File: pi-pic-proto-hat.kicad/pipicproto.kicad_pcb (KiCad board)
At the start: 2 copper layers, 65 x 56 mm, 20 parts, among them J1 RUN/~PGM~, J10 Conn_01x13_Male, J22 Conn_01x13_Male, J6 Barrel_Jack_Switch, J7 Conn_01x24_Male, J8 Conn_01x06_Male, J9 Conn_01x02_Male, P1 Conn_02x20_Odd_Even, Q1 IRF4905, U1 PIC12F675-IP

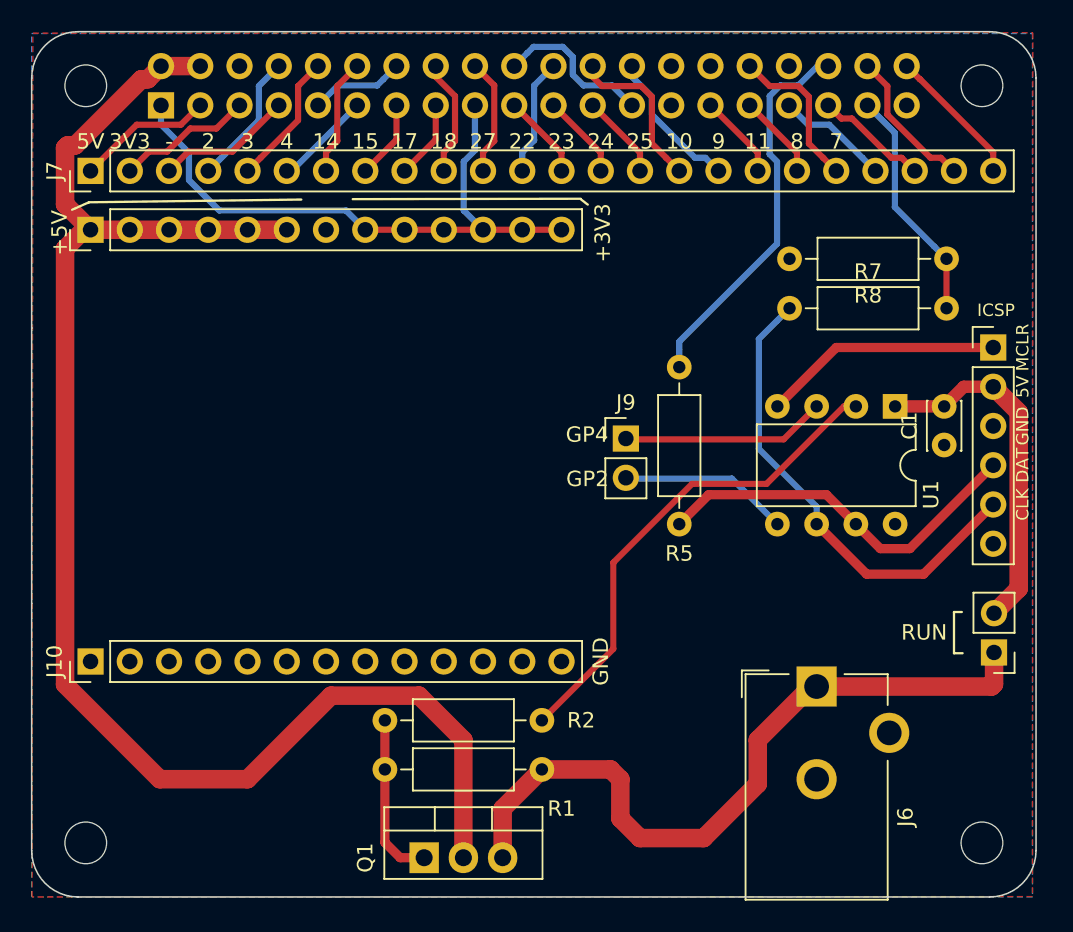
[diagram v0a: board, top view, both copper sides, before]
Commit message: V2.08: migrate to SMD for PIC
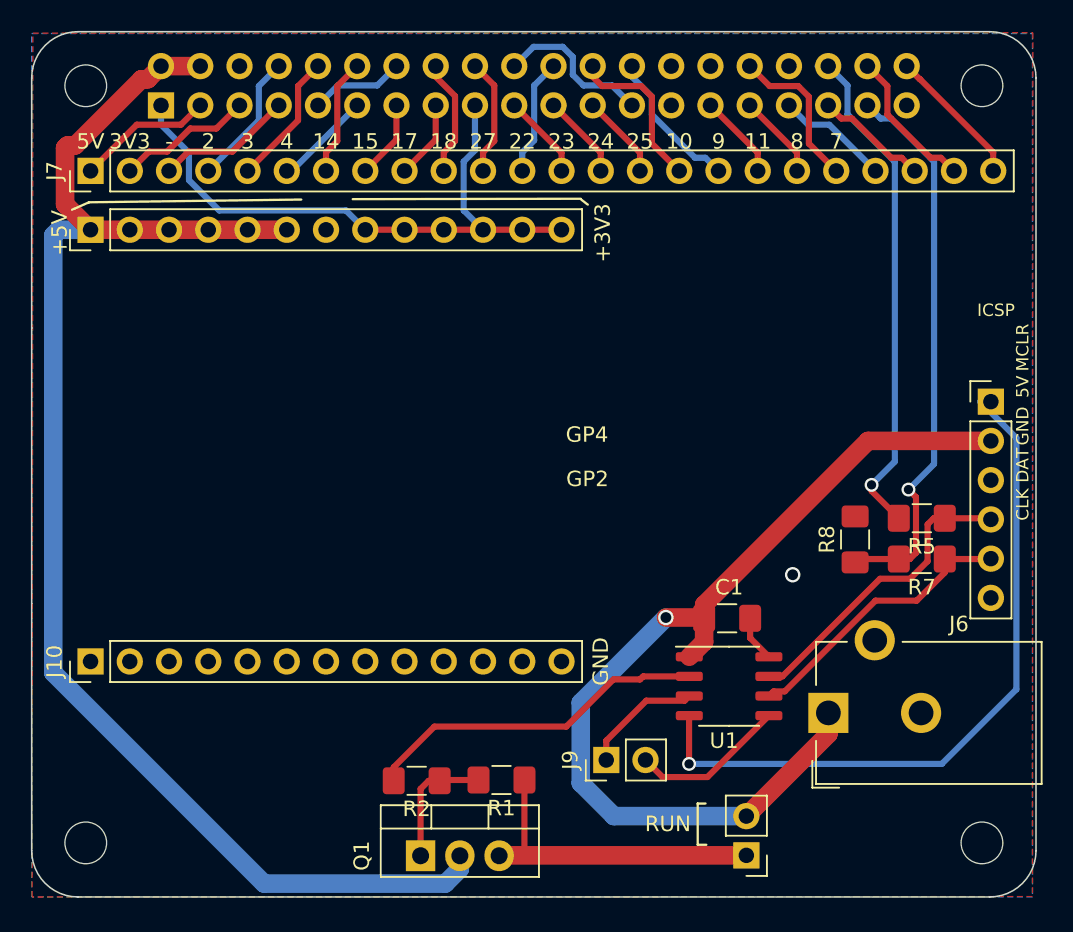
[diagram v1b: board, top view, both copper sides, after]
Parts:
- C1: footprint Capacitor_THT:C_Disc_D3.0mm_W2.0mm_P2.50mm -> Capacitor_SMD:C_1206_3216Metric_Pad1.42x1.75mm_HandSolder
- R1, R2, R5, R7, R8: footprint Resistor_THT:R_Axial_DIN0207_L6.3mm_D2.5mm_P10.16mm_Horizontal -> Resistor_SMD:R_1206_3216Metric_Pad1.42x1.75mm_HandSolder
- U1: footprint Package_DIP:DIP-8_W7.62mm -> Package_SO:SO-8_3.9x4.9mm_P1.27mm
- moved U1 21.1 mm to (245.1, 136.4), turned to 0 degrees
- moved J9 20.8 mm to (237.2, 141.1), turned to 90 degrees
- moved J1 20.7 mm to (246.3, 147.3)
- moved R8 19.1 mm to (253.3, 126.9), turned to 90 degrees
- moved R7 18.3 mm to (257.6, 128.1), turned to 180 degrees
- moved C1 18.0 mm to (245.0, 132.0), turned to 180 degrees
- moved R5 15.7 mm to (257.6, 125.5), turned to 180 degrees
- moved R2 4.42 mm to (224.9, 142.5), turned to 180 degrees
- moved J8 3.51 mm to (262.1, 117.9)
- moved R1 2.70 mm to (230.4, 142.4)
- moved J6 1.87 mm to (251.6, 138.1), turned to 90 degrees
- moved Q1 0.26 mm to (225.2, 147.3)
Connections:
- J6 pad 1: +5P -> +5VP
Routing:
- net +5VP: track 22.9 -> 62.7 mm, vias 0 -> 1
- net /MCLR: track 15.5 -> 46.6 mm, vias 0 -> 1
- net +5P: track 47.2 -> 22.4 mm
- net /GPIO26: track 15.2 -> 36.2 mm, vias 0 -> 1
- net /CLK: track 31.0 -> 18.6 mm
- net Net-(R2-Pad2): track 32.0 -> 22.4 mm
- net /GPIO16: track 25.0 -> 33.1 mm, vias 0 -> 1
- net +5V: track 99.4 -> 93.7 mm
- net Net-(J9-Pad1): track 12.8 -> 7.82 mm
- net /DAT: track 24.8 -> 20.0 mm
- net GND: track 16.5 -> 19.6 mm, vias 0 -> 1
- net Net-(Q1-Pad1): track 10.9 -> 8.77 mm
- net Net-(J9-Pad2): track 10.6 -> 10.1 mm

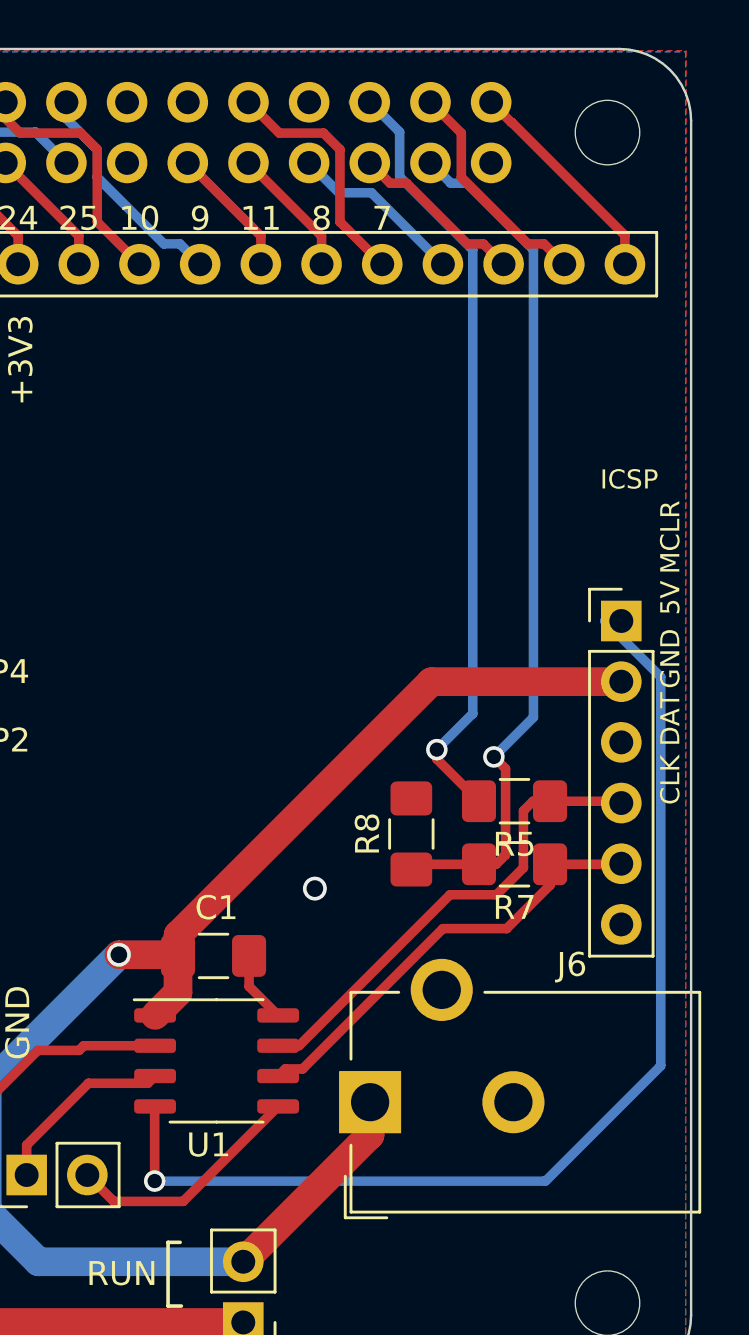
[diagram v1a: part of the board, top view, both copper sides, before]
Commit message: V2.09: rotated ICSP-header to optimze layout
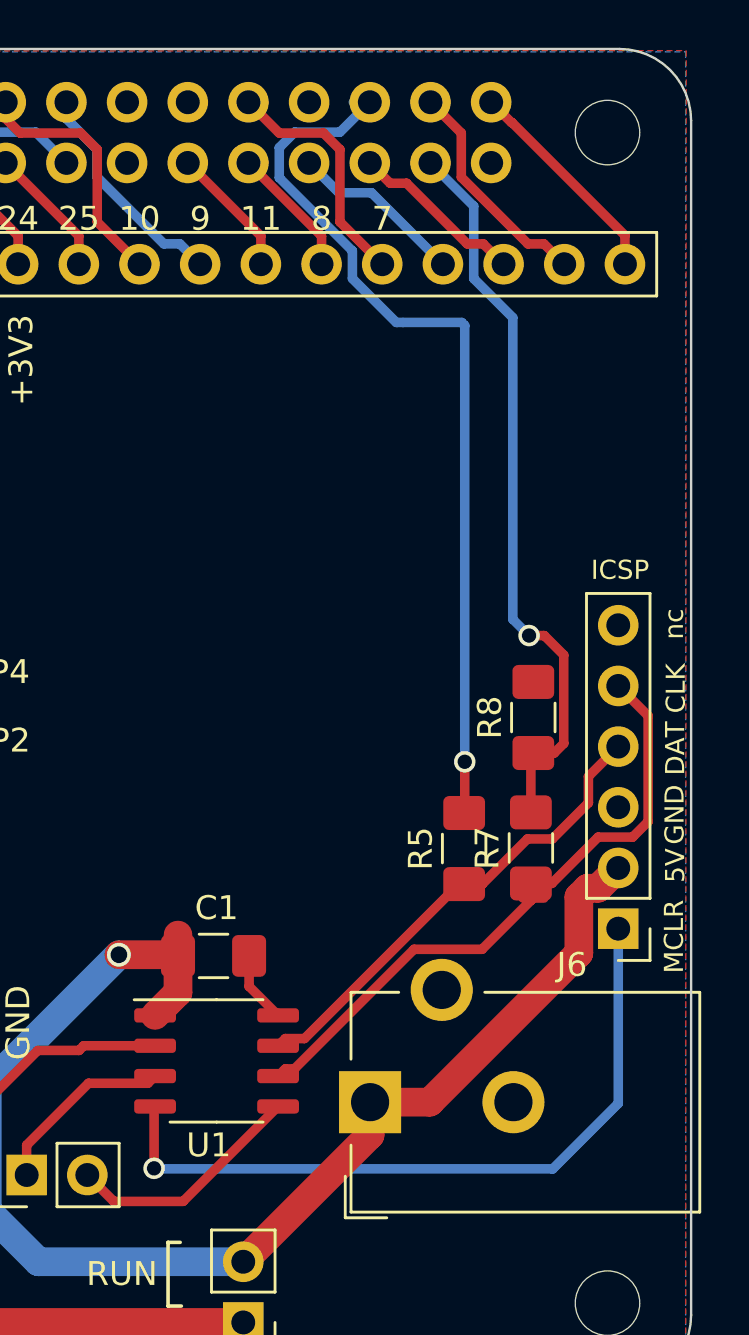
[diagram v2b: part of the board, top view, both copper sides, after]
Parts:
- moved J8 12.9 mm to (262.0, 130.8), turned to 180 degrees
- moved R8 7.06 mm to (258.4, 122.0)
- moved R5 2.89 mm to (255.5, 127.5), turned to 90 degrees
- moved R7 0.97 mm to (258.3, 127.4), turned to 90 degrees
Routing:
- net /MCLR: track 46.6 -> 30.5 mm
- net /CLK: track 18.6 -> 27.4 mm
- net +5VP: track 62.7 -> 55.6 mm
- net /GPIO16: track 33.1 -> 38.0 mm
- net /GPIO26: track 36.2 -> 31.4 mm
- net GND: vias 1 -> 0
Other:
- board text added: "nc"

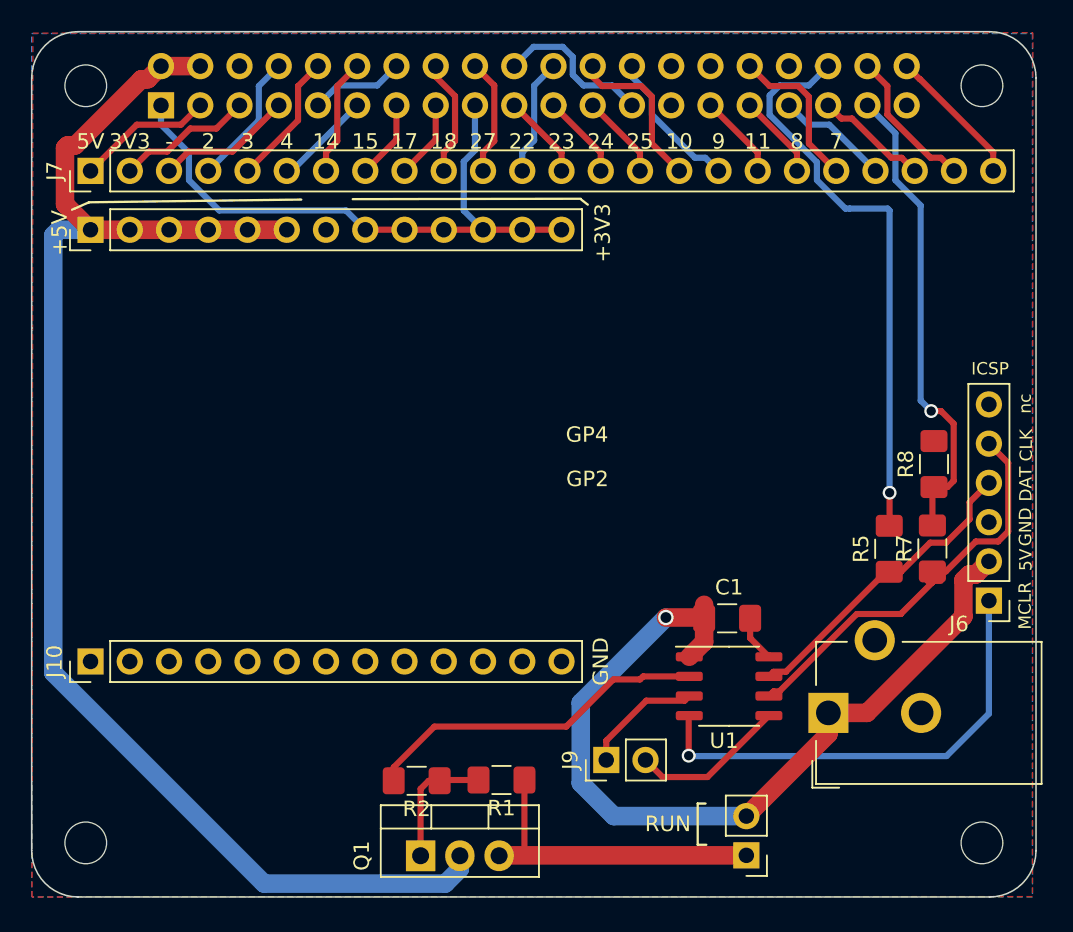
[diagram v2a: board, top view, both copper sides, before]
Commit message: V2.10: changed place of GP2/GP4 header
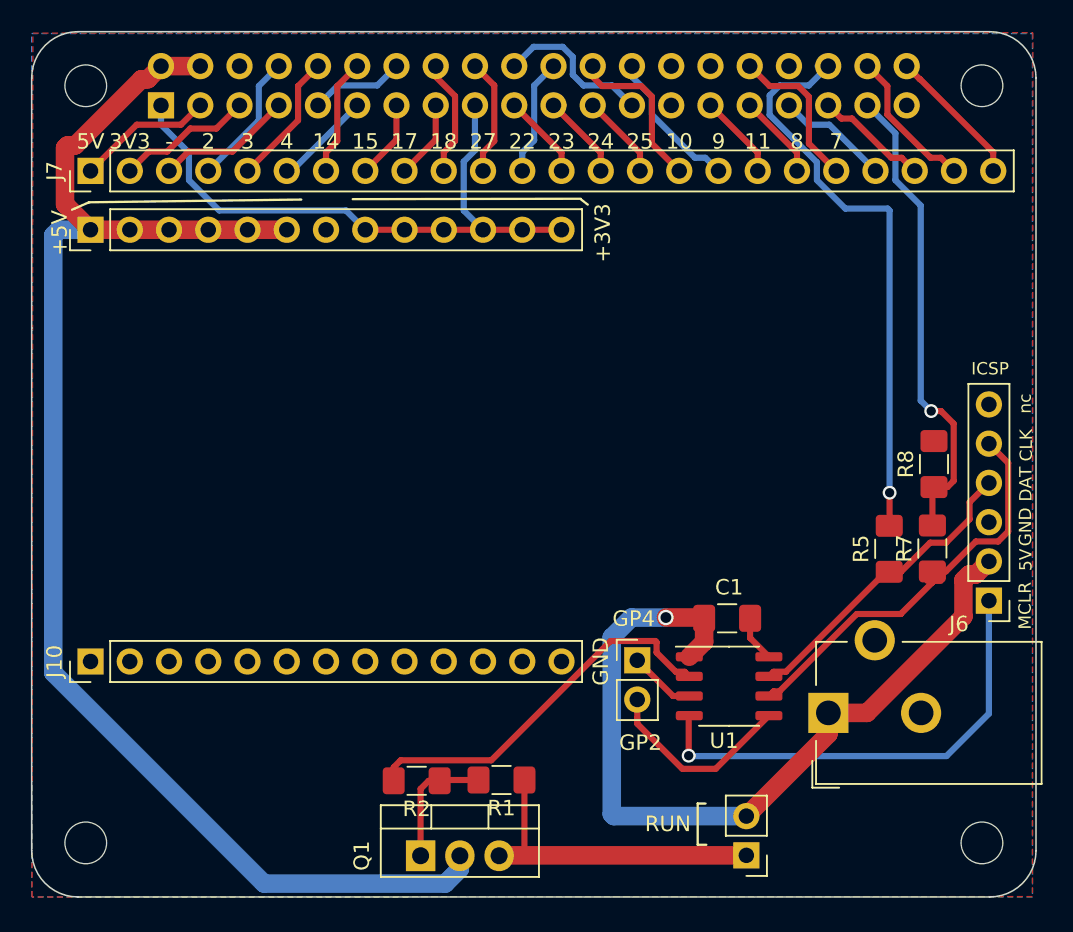
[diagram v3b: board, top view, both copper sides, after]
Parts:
- moved J9 6.76 mm to (239.2, 134.7), turned to 0 degrees
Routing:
- net Net-(J9-Pad1): track 7.82 -> 4.33 mm
- net Net-(J9-Pad2): track 10.1 -> 12.7 mm
- net Net-(R2-Pad2): track 22.4 -> 24.7 mm
- net +5VP: track 55.6 -> 54.3 mm
